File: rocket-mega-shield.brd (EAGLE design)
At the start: 114.3 x 60 mm, 62 parts, among them J1 ExtBatt, J2 MICROSD, J3 Mega R3, J4 1X6TERMINALBLOCK, J5 XBEE, Q1 BSS138, Q2 BSS138, Q3 SI7112DN, Q4 SI7112DN, Q5 SI7112DN, Q6 SI7112DN, Q7 BSS138, U1 BMP180, U2 FGPMMOPA6H, U3 NCP1117DT33G, U6 LSM303DLHCTR, U7 L3GD20TR, U8 ADXL377, U9 M74HC4050M

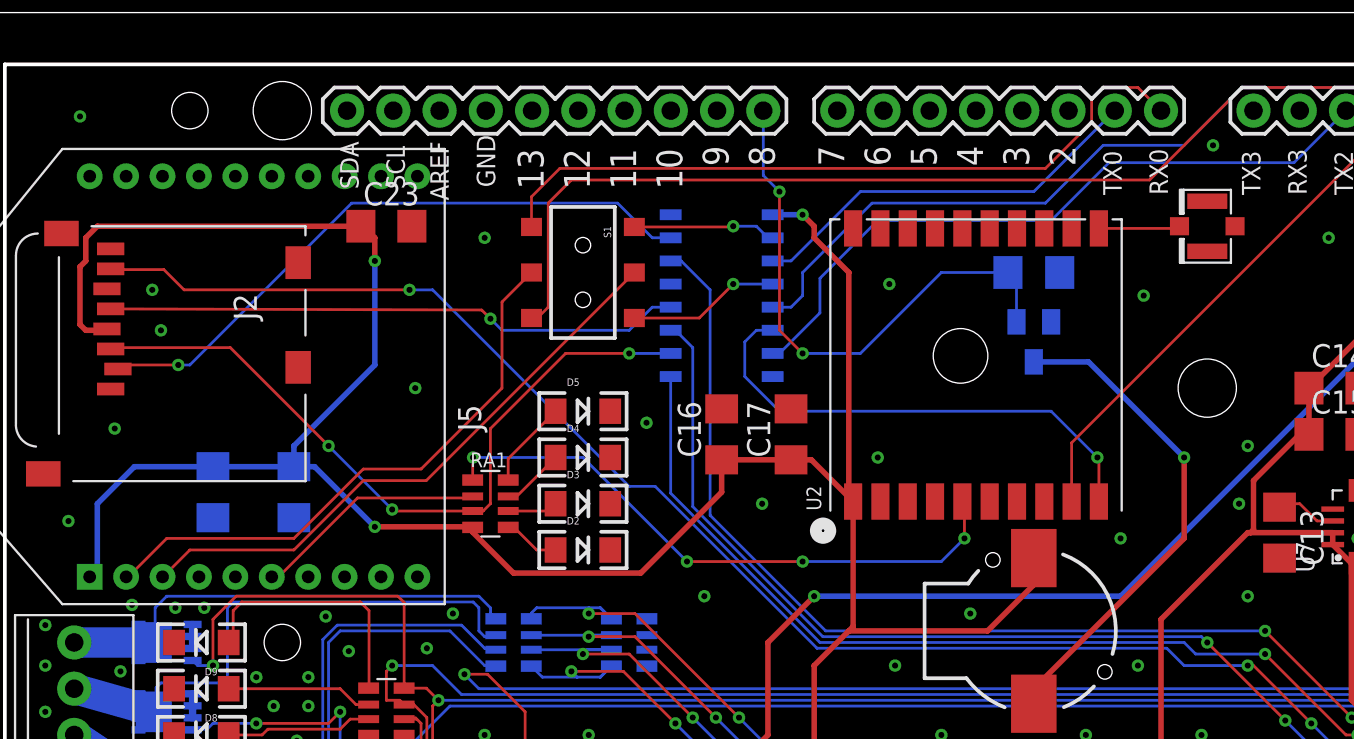
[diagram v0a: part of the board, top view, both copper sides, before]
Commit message: added LED on pin 13, more cleanup, updated BOM
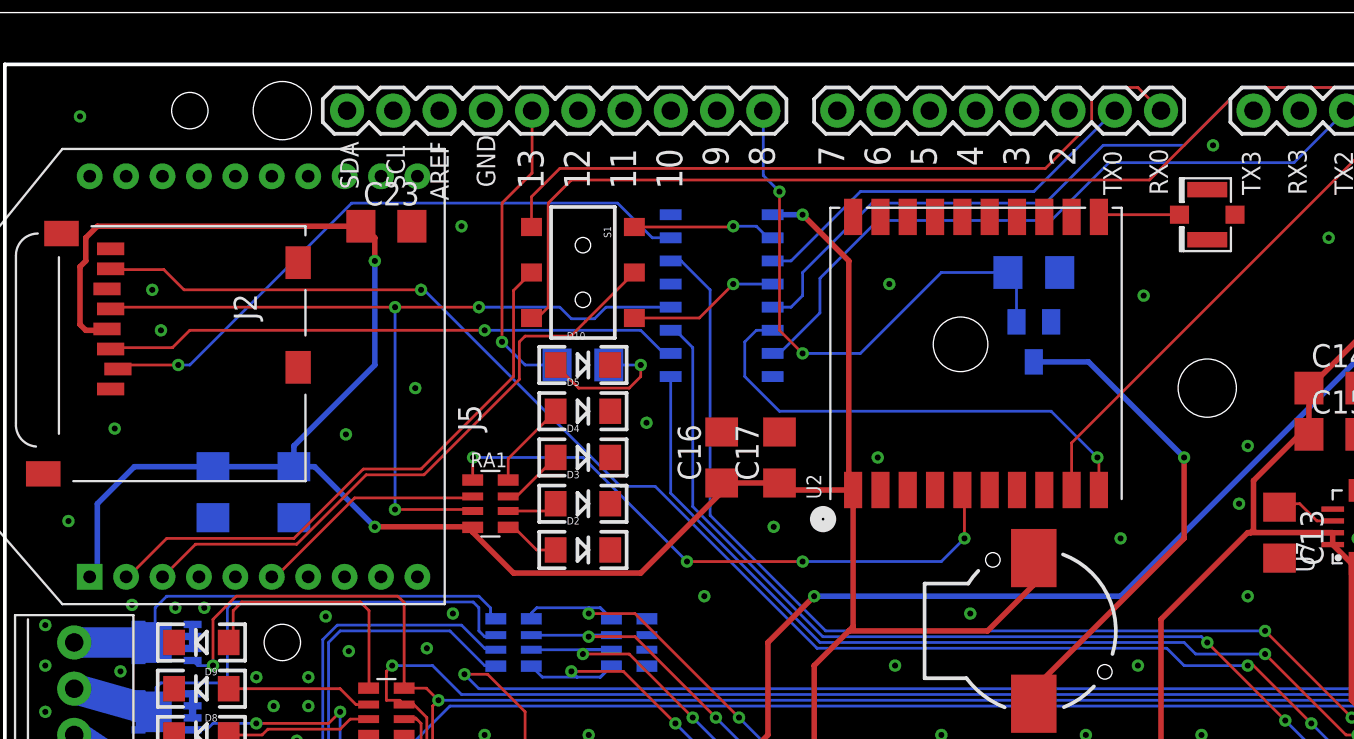
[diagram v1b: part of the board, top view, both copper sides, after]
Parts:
- removed GPS_EXT: U.FL, SparkFun-Connectors:U.FL
- added D10: 13 - red, SparkFun-LED:LED-1206
- added J6: U.FL, SparkFun-Connectors:U.FL
- added R4: 330, adafruit:R1206
- moved C17 1.42 mm to (51.4, 35.6)
- moved C16 1.27 mm to (48.3, 35.6)
- moved U2 0.63 mm to (62.2, 41.3)
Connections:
- new net N$14: D10.A, R4.2
- new net N$9: J3.13, R4.1
- net GND: now also D10.C, J6.P$1, J6.P$2; no longer GPS_EXT.P$1, GPS_EXT.P$2
- net MOSI: no longer RA1.3
- net N$10: now also J6.P$3; no longer GPS_EXT.P$3
- net SCLK: now also RA1.3
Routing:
- net N$9: track 0.00 -> 16.9 mm, vias 0 -> 1
- net SCLK: track 31.7 -> 46.7 mm, vias 1 -> 3
- net MOSI: track 40.5 -> 31.7 mm, vias 3 -> 1
- net N$14: track 0.00 -> 7.85 mm, vias 0 -> 1
- net VCC3: track 303.9 -> 302.6 mm
- net N$22: track 32.8 -> 34.0 mm
- net TX2: track 27.4 -> 26.7 mm
- net MEGARX2: track 28.8 -> 28.1 mm
- net GPSFIX: track 33.2 -> 33.8 mm
- net GND: vias 72 -> 73

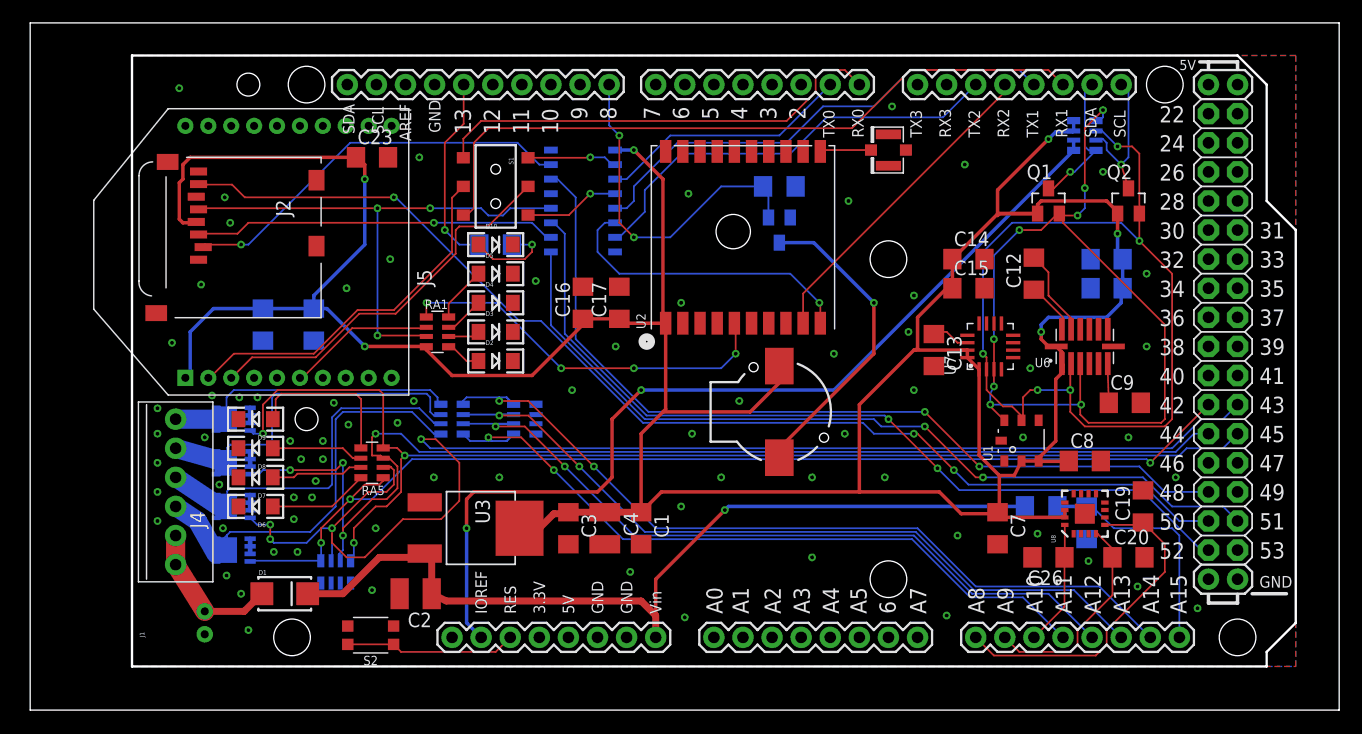
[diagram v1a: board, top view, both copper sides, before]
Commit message: routing and visual cleanup
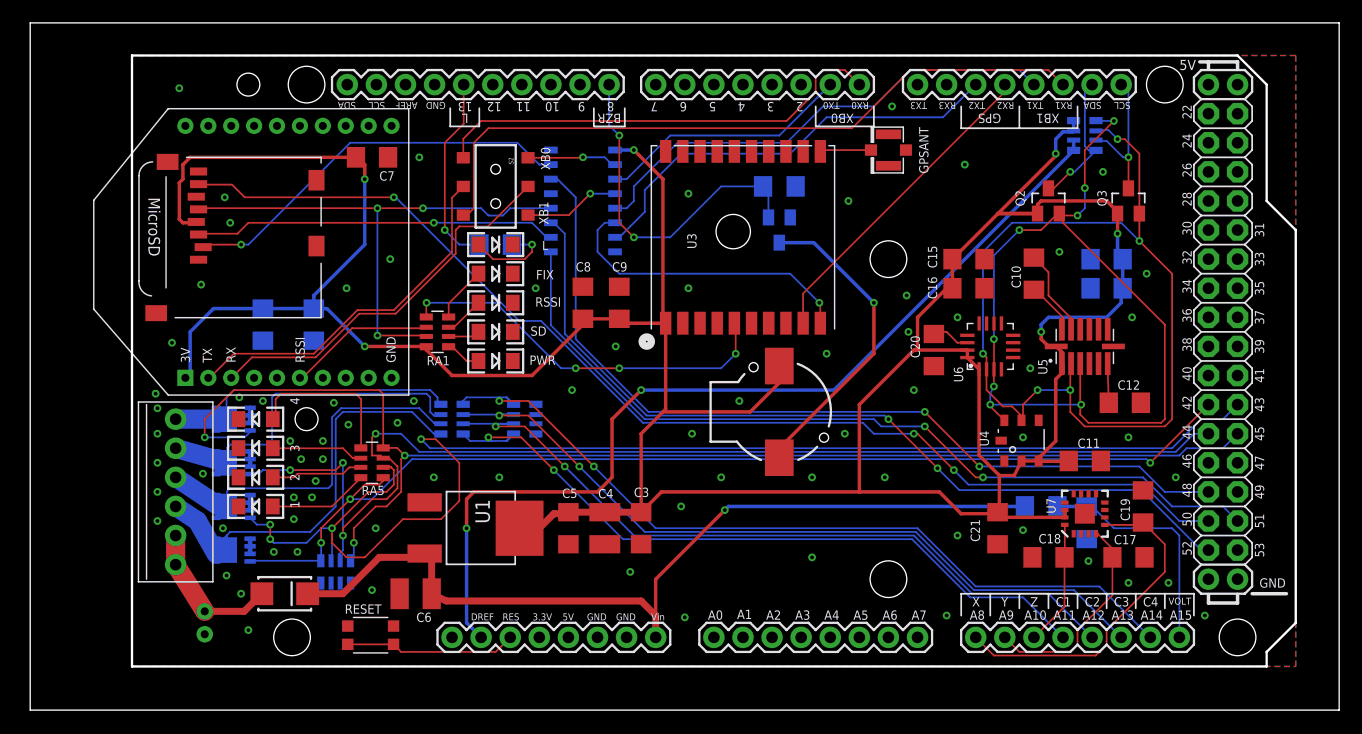
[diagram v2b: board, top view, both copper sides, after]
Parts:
- removed C22, C23: 0.1uF, adafruit:C1206
- removed U8: ADXL377, zortness:LFCSP-16
- removed U9: M74HC4050M, SparkFun-DigitalIC:SO016
- added C5: 10uF, adafruit:C1206
- added C6: 100uF16V, adafruit:C1210
- added U4: BMP180, zortness:BMP180
- added U5: LSM303DLHCTR, kurt:LGA14
- C1: value 100uF -> 10uF
- C10: value 10uF -> 0.22uF
- C12: value 0.22uF -> 4.7uF
- C13: value 0.01uF -> 10uF
- C14, C21: value 10uF -> 0.1uF
- C15: value 0.1uF -> 10uF
- C16: value 1uF -> 0.1uF
- C2: value 100uF16V -> 0.1uF; device adafruit:C1210 -> adafruit:C1206
- C3: value 10uF -> 100uF
- C8: value 0.1uF -> 1uF
- C9: value 4.7uF -> 0.01uF
- D10: value 13 - red -> Pyro4 - red
- D2: value PWR - green -> 13 - red
- D3: value SDAct - orange -> Fix - blue
- D5: value Fix - blue -> SDAct - orange
- D6: value Pyro1 - red -> PWR - green
- D7: value Pyro2 - red -> Pyro1 - red
- D8: value Pyro3 - red -> Pyro2 - red
- D9: value Pyro4 - red -> Pyro3 - red
- J2: value MICROSD -> Mega R3; device zortness:MICROSD -> zortness:ARDUINO_MEGA
- J3: value Mega R3 -> XBEE; device kurt:ARDUINO_MEGA -> adafruit:XBEE
- J4: value 1X6TERMINALBLOCK -> MICROSD; device zortness:1X6TERMINALBLOCK -> zortness:MICROSD
- J5: value XBEE -> U.FL; device adafruit:XBEE -> SparkFun-Connectors:U.FL
- J6: value U.FL -> 1X6TERMINALBLOCK; device SparkFun-Connectors:U.FL -> zortness:1X6TERMINALBLOCK
- Q3: value SI7112DN -> BSS138; device SparkFun-DiscreteSemi:POWERPAK1212-8 -> kurt:SOT23
- Q7: value BSS138 -> SI7112DN; device kurt:SOT23 -> SparkFun-DiscreteSemi:POWERPAK1212-8
- R1, RA3: value 620k -> 110k
- R2, RA4: value 110k -> 620k
- R3: value 10k -> 330
- R4: value 330 -> 10k
- S1: value AYZ0202 -> KMR2; device SparkFun-Electromechanical:AYZ0202 -> zortness:TACTILE_KMR2
- S2: value KMR2 -> AYZ0202; device zortness:TACTILE_KMR2 -> SparkFun-Electromechanical:AYZ0202
- U1: value BMP180 -> NCP1117DT33G; device zortness:BMP180 -> kurt:DPAK
- U2: value FGPMMOPA6H -> M74HC4050M; device adafruit:FGPMMOPA6H -> SparkFun-DigitalIC:SO016
- U3: value NCP1117DT33G -> FGPMMOPA6H; device kurt:DPAK -> adafruit:FGPMMOPA6H
- U6: value LSM303DLHCTR -> L3GD20TR; device kurt:LGA14 -> kurt:LGA16-4X4
- U7: value L3GD20TR -> ADXL377; device kurt:LGA16-4X4 -> zortness:LFCSP-16
- moved Q3 83.8 mm to (95.9, 44.5), flipped to the top
- moved RA2 75.7 mm to (26.7, 12.1), turned to 180 degrees
- moved RA6 75.7 mm to (92.1, 50.2), turned to 90 degrees
- moved J6 69.0 mm to (12.7, 19.1), turned to 90 degrees
- moved C21 66.6 mm to (84.5, 15.9), flipped to the top
- moved C7 63.5 mm to (29.8, 48.3), turned to 0 degrees
- moved J5 56.6 mm to (74.9, 48.9), turned to 180 degrees
- moved Q7 55.2 mm to (17.8, 14.0), turned to 0 degrees
- moved C17 49.7 mm to (95.9, 13.3), turned to 0 degrees
- moved J2 47.4 mm to (8.89, 3.81), turned to 0 degrees
- moved C8 45.9 mm to (48.3, 35.6), turned to 90 degrees
- moved U1 45.8 mm to (39.4, 15.9), turned to 270 degrees
- moved C9 45.0 mm to (51.4, 35.6), turned to 90 degrees
- moved S1 41.3 mm to (32.2, 5.24), turned to 180 degrees
- moved S2 41.3 mm to (40.6, 45.7), turned to 270 degrees
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- renumbered C26 to C18
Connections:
- net BATT+: now also J6.1, J6.2; no longer J4.1, J4.2
- net GND: now also C12.2, C5.2, C6.2, J2.GND@0, J2.GND@1, J2.GND@2, J2.GND@3, J2.GND@4, J3.10, J4.6, J4.CD1, J4.CD2, J4.MT1, J4.MT2, J5.P$1, J5.P$2, Q1.2, Q7.S1, Q7.S2, Q7.S3, R1.1, R4.2, RA2.5, RA2.6, RA2.7, RA2.8, RA3.1, RA3.2, RA3.3, RA3.4, S1.3, S1.4, U1.1, U2.8, U3.P$12, U3.P$19, U3.P$3, U3.P$8, U4.7, U5.10, U5.11, U5.7, U6.P$10, U6.P$11, U6.P$12, U6.P$13, U6.P$8, U6.P$9, U7.6, U7.7; no longer C10.2, C22.2, C23.2, J2.6, J2.CD1, J2.CD2, J2.MT1, J2.MT2, J3.GND@0, J3.GND@1, J3.GND@2, J3.GND@3, J3.GND@4, J5.10, J6.P$1, J6.P$2, Q3.S1, Q3.S2, Q3.S3, Q7.2, R2.1, R3.2, RA4.1, RA4.2, RA4.3, RA4.4, RA6.5, RA6.6, RA6.7, RA6.8, S2.3, S2.4, U1.7, U2.P$12, U2.P$19, U2.P$3, U2.P$8, U3.1, U6.10, U6.11, U6.7, U7.P$10, U7.P$11, U7.P$12, U7.P$13, U7.P$8, U7.P$9, U8.6, U8.7, U9.8
- net GPSFIX: now also U3.P$5; no longer U2.P$5
- net IOREF: now also J2.IOREF, RA6.1, RA6.2; no longer J3.IOREF, RA2.1, RA2.2
- net MEGA5V: now also J2.5V@0; no longer J3.5V@0
- net MEGA8: now also J2.8, Q1.1, R4.1; no longer J3.8, Q7.1, R3.1
- net MEGAA0: now also J2.A0; no longer J3.A0
- net MEGAA1: now also J2.A1; no longer J3.A1
- net MEGAA10: now also J2.A10, U7.16; no longer J3.A10, U8.16
- net MEGAA11: now also J2.A11, RA3.5, RA4.4; no longer J3.A11, RA3.4, RA4.5
- net MEGAA12: now also J2.A12, RA3.6, RA4.3; no longer J3.A12, RA3.3, RA4.6
- net MEGAA13: now also J2.A13, RA3.7, RA4.2; no longer J3.A13, RA3.2, RA4.7
- net MEGAA14: now also J2.A14, RA3.8, RA4.1; no longer J3.A14, RA3.1, RA4.8
- net MEGAA15: now also J2.A15, R1.2, R2.1; no longer J3.A15, R1.1, R2.2
- net MEGAA2: now also J2.A2; no longer J3.A2
- net MEGAA3: now also J2.A3; no longer J3.A3
- net MEGAA4: now also J2.A4; no longer J3.A4
- net MEGAA5: now also J2.A5; no longer J3.A5
- net MEGAA6: now also J2.A6; no longer J3.A6
- net MEGAA7: now also J2.A7; no longer J3.A7
- net MEGAA8: now also J2.A8, U7.5; no longer J3.A8, U8.5
- net MEGAA9: now also C17.1, J2.A9, U7.4; no longer C20.1, J3.A9, U8.4
- net MEGAMISO: now also J2.50, J4.7; no longer J2.7, J3.50
- net MEGAMOSI: now also J2.51, U2.9; no longer J3.51, U9.9
- net MEGARX0: now also J2.0, S2.4; no longer J3.0, S1.4
- net MEGARX1: now also J2.19, S2.6; no longer J3.19, S1.6
- net MEGARX2: now also J2.17, U3.P$9; no longer J3.17, U2.P$9
- net MEGASCL: now also J2.21, Q3.3, RA6.7; no longer J3.21, Q2.3, RA2.7
- net MEGASCLK: now also J2.52, U2.11; no longer J3.52, U9.11
- net MEGASDA: now also J2.20, Q2.3, RA6.8; no longer J3.20, Q1.3, RA2.8
- net MEGASDCS: now also J2.48, U2.14; no longer J3.48, U9.14
- net MEGATX0: now also J2.1, U2.3; no longer J3.1, U9.3
- net MEGATX1: now also J2.18, U2.5; no longer J3.18, U9.5
- net MEGATX2: now also J2.16, U2.7; no longer J3.16, U9.7
- net MOSI: now also J4.3, U2.10; no longer J2.3, U9.10
- net N$1: now also D6.A; no longer D2.A
- net N$10: now also J5.P$3, U3.P$11; no longer J6.P$3, U2.P$11
- net N$12: now also D3.A; no longer D5.A
- net N$13: now also Q1.3; no longer Q7.3
- net N$14: now also D2.A, R3.2; no longer D10.A, R4.2
- net N$16: now also D10.A; no longer D9.A
- net N$17: now also D9.A; no longer D8.A
- net N$18: now also D8.A; no longer D7.A
- net N$19: now also D7.A; no longer D6.A
- net N$2: now also D5.A; no longer D3.A
- net N$21: now also J3.2, S2.5; no longer J5.2, S1.5
- net N$22: now also J3.3, S2.2; no longer J5.3, S1.2
- net N$24: now also J6.6, Q5.D1, Q5.D2, Q5.D3, Q5.D4, Q5.DPAD, RA4.8; no longer J4.6, Q6.D1, Q6.D2, Q6.D3, Q6.D4, Q6.DPAD, RA3.8
- net N$25: now also J6.5, Q6.D1, Q6.D2, Q6.D3, Q6.D4, Q6.DPAD, RA4.7; no longer J4.5, Q5.D1, Q5.D2, Q5.D3, Q5.D4, Q5.DPAD, RA3.7
- net N$3: now also J6.3, Q7.D1, Q7.D2, Q7.D3, Q7.D4, Q7.DPAD, RA4.5; no longer J4.3, Q3.D1, Q3.D2, Q3.D3, Q3.D4, Q3.DPAD, RA3.5
- net N$4: now also J6.4, RA4.6; no longer J4.4, RA3.6
- net N$5: now also C10.2, U5.12; no longer C12.2, U6.12
- net N$6: now also C10.1, U5.13; no longer C12.1, U6.13
- net N$7: now also C12.1, U5.6; no longer C9.1, U6.6
- net N$8: now also C20.1, U6.P$14; no longer C13.1, U7.P$14
- net N$9: now also J2.13, R3.1; no longer J3.13, R4.1
- net PYRO1: now also J2.42, Q7.G, RA2.1; no longer J3.42, Q3.G, RA6.1
- net PYRO2: now also J2.43, RA2.2; no longer J3.43, RA6.2
- net PYRO3: now also J2.44, Q6.G, RA2.3; no longer J3.44, Q5.G, RA6.3
- net PYRO4: now also J2.45, Q5.G, RA2.4; no longer J3.45, Q6.G, RA6.4
- net RESET: now also J2.RESET, S1.1, S1.2; no longer J3.RESET, S2.1, S2.2
- net SCL: now also Q3.2, RA6.6, U4.5, U5.2, U6.P$2; no longer Q2.2, RA2.6, U1.5, U6.2, U7.P$2
- net SCLK: now also J4.5, U2.12; no longer J2.5, U9.12
- net SDA: now also Q2.2, RA6.5, U4.6, U5.3, U6.P$3; no longer Q1.2, RA2.5, U1.6, U6.3, U7.P$3
- net SDCS: now also J4.2, U2.15; no longer J2.2, U9.15
- net TX0: now also S2.1, U2.2; no longer S1.1, U9.2
- net TX1: now also S2.3, U2.4; no longer S1.3, U9.4
- net TX2: now also U2.6, U3.P$10; no longer U2.P$10, U9.6
- net VCC3: now also C13.1, C2.1, C5.1, C9.1, J3.1, J4.4, Q3.1, RA6.3, RA6.4, U1.4, U2.1, U3.P$1, U4.2, U4.3, U5.1, U5.14, U6.P$1, U6.P$15, U6.P$16, U7.14, U7.15; no longer C10.1, C17.1, C22.1, C23.1, J2.4, J5.1, Q1.1, RA2.3, RA2.4, U1.2, U1.3, U2.P$1, U3.4, U6.1, U6.14, U7.P$1, U7.P$15, U7.P$16, U8.14, U8.15, U9.1
- net VIN: now also C6.1, J2.VIN, R2.2, U1.3; no longer C2.1, J3.VIN, R1.2, U3.3
- net XRSSI: now also J3.6; no longer J5.6
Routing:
- net PYRO4: track 107.4 -> 115.1 mm
- net VCC3: track 302.6 -> 301.8 mm
- net GND: vias 73 -> 75
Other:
- board text added: "1"
- board text added: "2"
- board text added: "3"
- board text added: "3V"
- board text added: "4"
- board text added: "BZR"
- board text added: "C1"
- board text added: "C2"
- board text added: "C3"
- board text added: "C4"
- board text added: "FIX"
- board text added: "GND"
- board text added: "GPS"
- board text added: "GPSANT"
- board text added: "L"
- board text added: "MicroSD"
- board text added: "PWR"
- board text added: "RESET"
- board text added: "RSSI"
- board text added: "RX"
- board text added: "SD"
- board text added: "TX"
- board text added: "VOLT"
- board text added: "X"
- board text added: "XB0"
- board text added: "XB1"
- board text added: "Y"
- board text added: "Z"
